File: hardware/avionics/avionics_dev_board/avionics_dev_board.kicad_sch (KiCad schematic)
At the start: 78 parts, among them IC1 ADXL375BCCZ, IC2 W25Q256JVEIQ, J1 Main battery, J10 Parachute battery, J2 LAMBDA62, J3 Conn_01x08_Socket, J4 LAMBDA80, J5 Conn_01x08_Socket, J6 SWD interface, J7 868MHz antenna, J8 2.4GHz antenna, J9 Nichrome connector, Q1 Q_NMOS, SW1 SW_Push, SW2 SW_Push, SW3 SW_Push, SW4 SW_Push, U1 TPS563200, U2 MMC5983MA, U3 LSM6DSR, U4 BMP581, U6 MAX-M10S-00B, U7 STM32G474RET6, Y1 8MHz

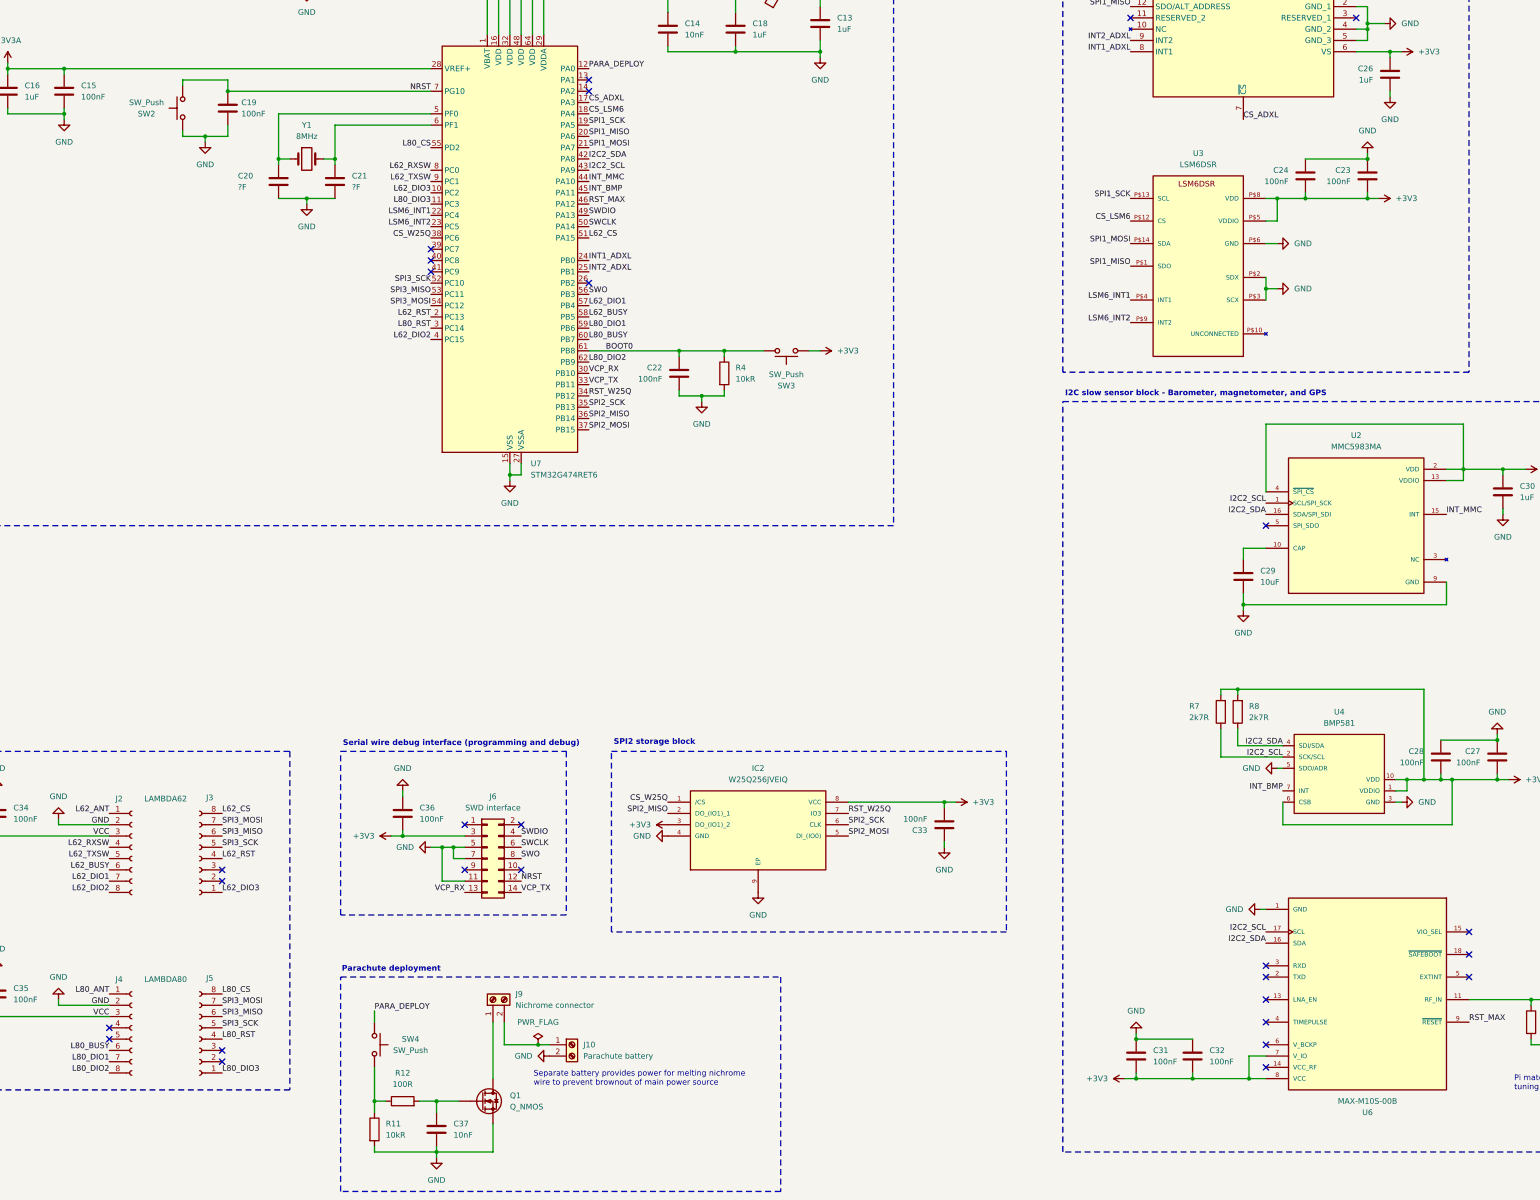
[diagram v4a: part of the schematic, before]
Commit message: Updated component selections and footprints assigned
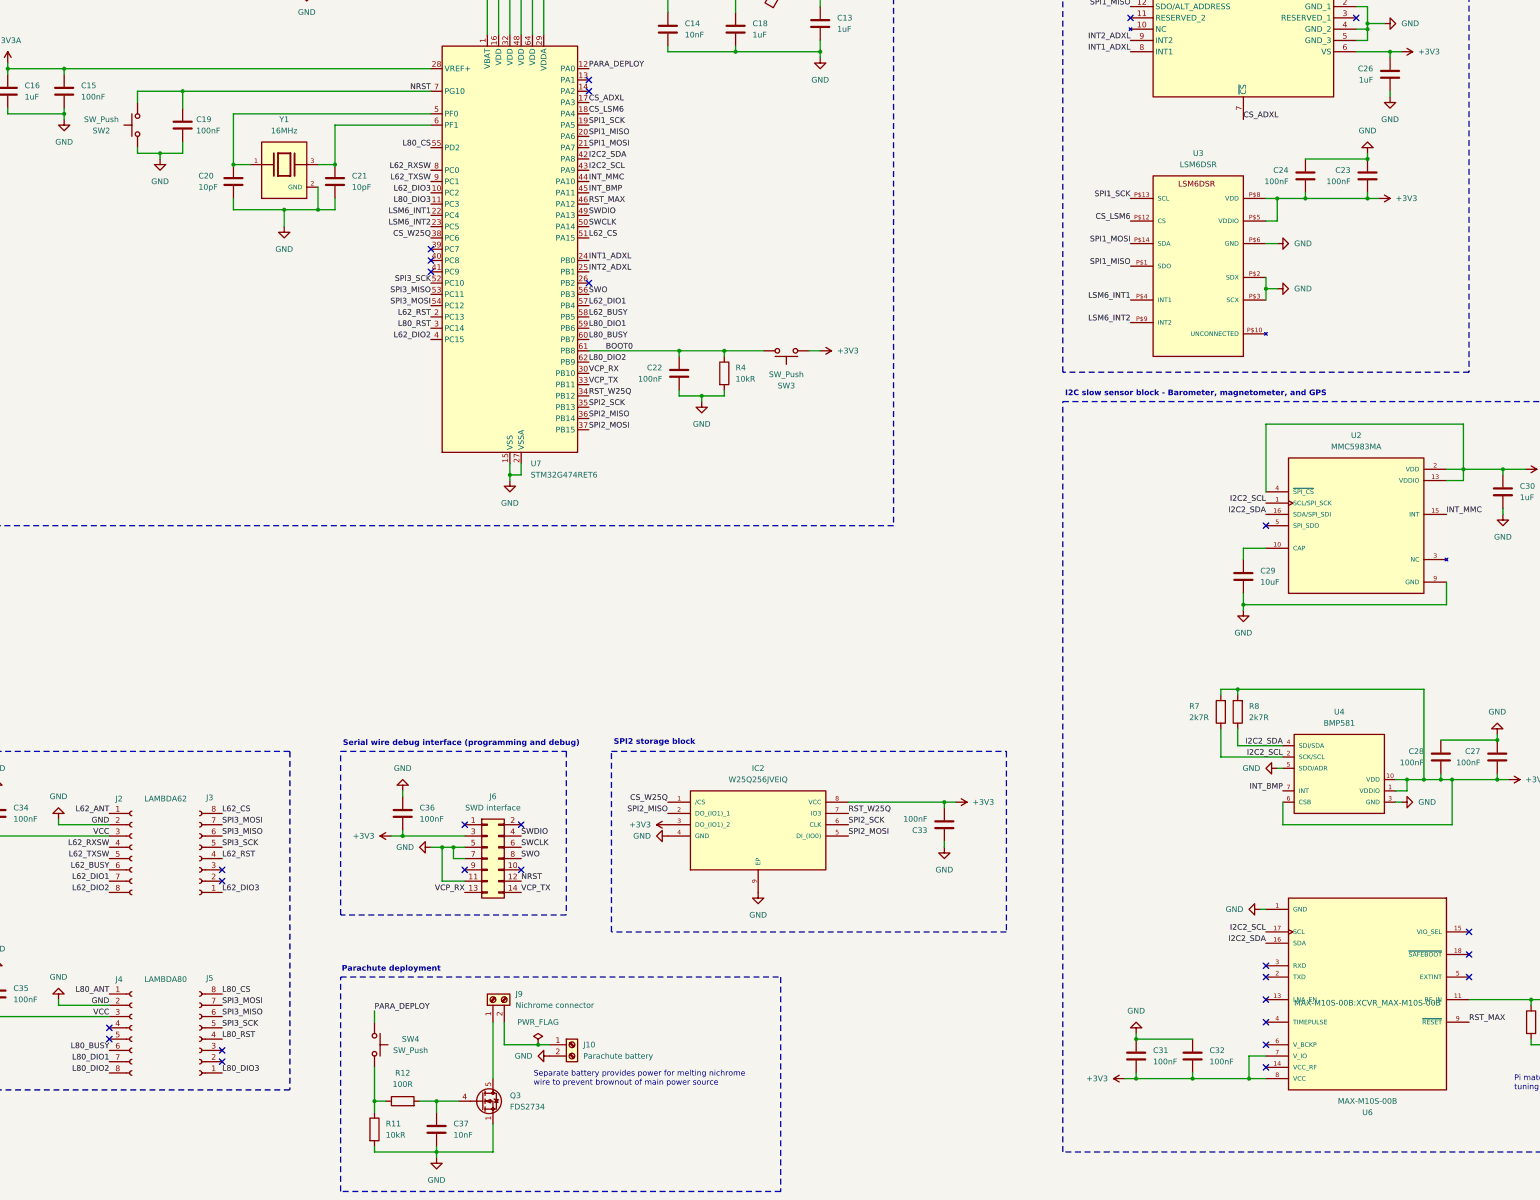
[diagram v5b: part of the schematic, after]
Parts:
- removed Q1: Q_NMOS, symbol Device:Q_NMOS
- removed Y1: 8MHz, symbol Device:Crystal
- added Q3: FDS2734, Package_SO:SOIC-8_3.9x4.9mm_P1.27mm, symbol Transistor_FET:FDS2734
- added Y1: 16MHz, ABM8G-16.000MHZ-4Y-T3:XTAL_ABM8G-16.000MHZ-4Y-T3, symbol ABM8G-16.000MHZ-4Y-T3:ABM8G-16.000MHZ-4Y-T3
- C1, C2, C8, C9: footprint Capacitor_SMD:C_0603_1608Metric -> Capacitor_SMD:C_0805_2012Metric
- C10, C11, C12, C13, C14, C15, C16, C17, C18, C19, C22, C23, C24, C25, C26, C27, C28, C29, C30, C31, C32, C33, C34, C35, C36, C37, C5: footprint (none) -> Capacitor_SMD:C_0603_1608Metric
- C20, C21: value ?F -> 10pF; footprint (none) -> Capacitor_SMD:C_0603_1608Metric
- C6: footprint (none) -> Capacitor_SMD:C_0805_2012Metric
- D1: footprint (none) -> LED_SMD:LED_0603_1608Metric
- D2: footprint (none) -> Diode_SMD:D_SOD-123F
- F1: footprint (none) -> Fuse:Fuse_0603_1608Metric
- FB1: footprint (none) -> Inductor_SMD:L_0603_1608Metric
- IC1: footprint (none) -> ADXL375:CC-14-1
- J6: footprint (none) -> Connector_PinHeader_2.54mm:PinHeader_2x07_P2.54mm_Vertical
- J7, J8: footprint (none) -> Connector_Coaxial:SMA_Amphenol_901-144_Vertical
- L1: footprint Inductor_SMD:L_Coilcraft_1515SQ-68N -> Inductor_SMD:L_0805_2012Metric
- R11, R12, R13, R14, R15, R4, R7, R8: footprint (none) -> Resistor_SMD:R_0603_1608Metric
- SW2: footprint Button_Switch_SMD:SW_DIP_SPSTx01_Slide_6.7x4.1mm_W6.73mm_P2.54mm_LowProfile_JPin -> Button_Switch_SMD:SW_SPST_B3U-1000P
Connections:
- net GND: now also Q3.1 (S), Q3.2 (S), Q3.3 (S), Y1.2 (GND), Y1.4 (GND)
- net at J9.1 (Pin_1): now also Q3.5 (D), Q3.6 (D), Q3.7 (D), Q3.8 (D)
- net at C37.1, R12.2: now also Q3.4 (G)
- net at C20.1, U7.5 (PF0): now also Y1.1
- net at C21.1, U7.6 (PF1): now also Y1.3
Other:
- moved on the sheet: C19, C20, SW2

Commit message: First revision of avionics dev board PCB - needs routing fixes
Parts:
- removed SW1, SW3: SW_Push, Button_Switch_SMD:SW_DIP_SPSTx01_Slide_6.7x4.1mm_W6.73mm_P2.54mm_LowProfile_JPin, symbol Switch:SW_Push
- removed SW2: SW_Push, Button_Switch_SMD:SW_SPST_B3U-1000P, symbol Switch:SW_Push
- added SW2, SW3, SW5: SW_SPDT, avionicsw:SHOU HAN SS12D10G5, symbol Switch:SW_SPDT
- F1: value 2A -> 1A
- SW4: footprint Button_Switch_SMD:SW_DIP_SPSTx01_Slide_6.7x4.1mm_W6.73mm_P2.54mm_LowProfile_JPin -> avionicsw:G-Switch GT-TC060A-H025-L1S
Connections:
- net +3V3: now also U7.1 (VBAT), U7.16 (VDD), U7.32 (VDD), U7.48 (VDD), U7.64 (VDD), SW2.2 (B)
- net BOOT0: now also SW2.3 (C)
- net GND: now also SW4.1; no longer U7.1 (VBAT), U7.16 (VDD), U7.32 (VDD), U7.48 (VDD), U7.64 (VDD)
- net NRST: now also SW4.2
- net PARA_DEPLOY: now also SW3.2 (B); no longer SW4.1
- net at C3.2, D2.1 (K): now also U1.3 (VIN), U1.5 (EN)
- net at C1.2, F1.1: now also SW5.1 (A); no longer J1.2 (Pin_2)
- net at R11.1, R12.1: now also SW3.3 (C); no longer SW4.2
- new net: J1.2 (Pin_2), SW5.2 (B)
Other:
- moved on the sheet: C1, C10, C11, C12, C17, C2, C3, C5, C6, D2, F1, J1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

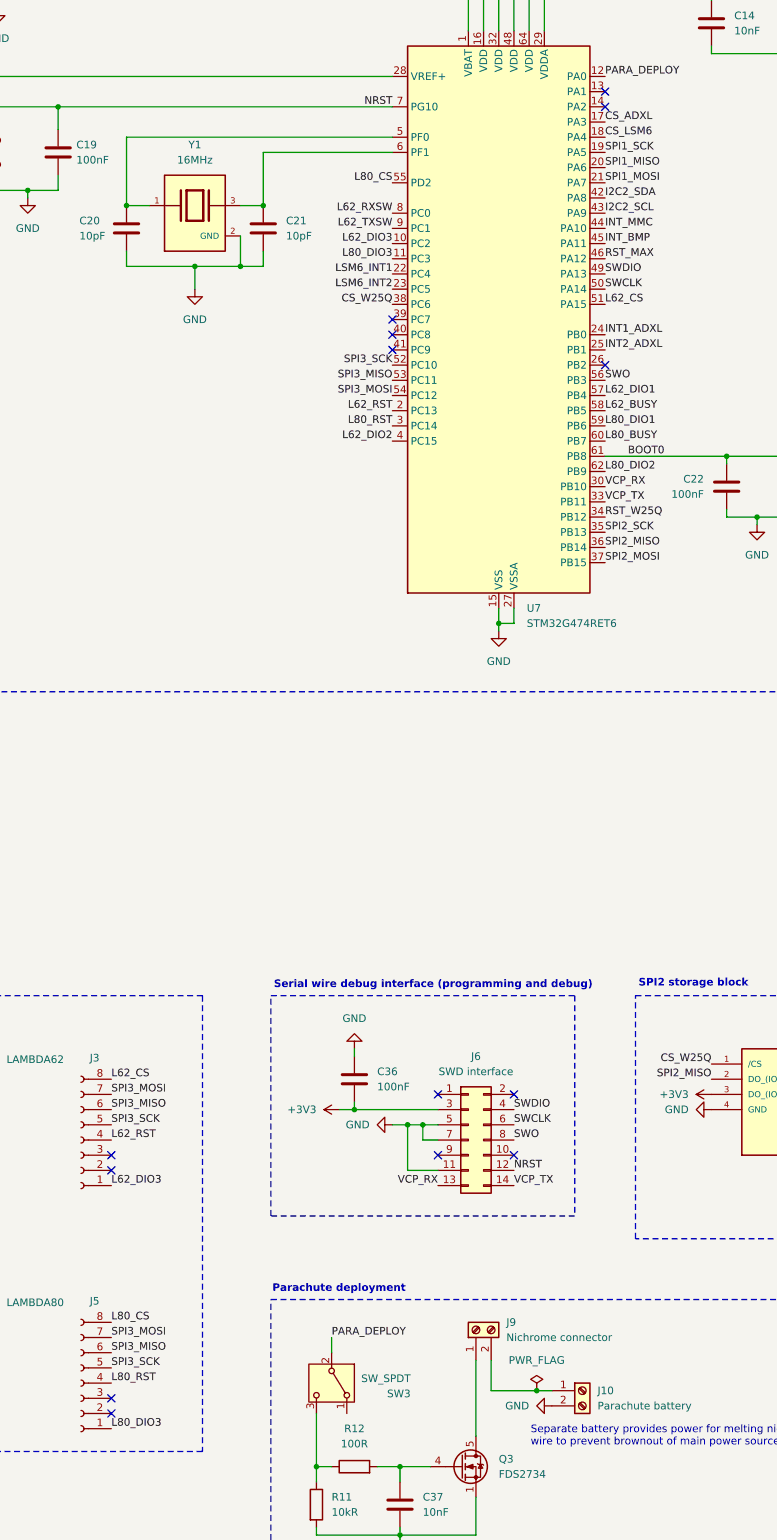
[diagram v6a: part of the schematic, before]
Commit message: Avionics dev PCB revision 2 - improved stackup and routing
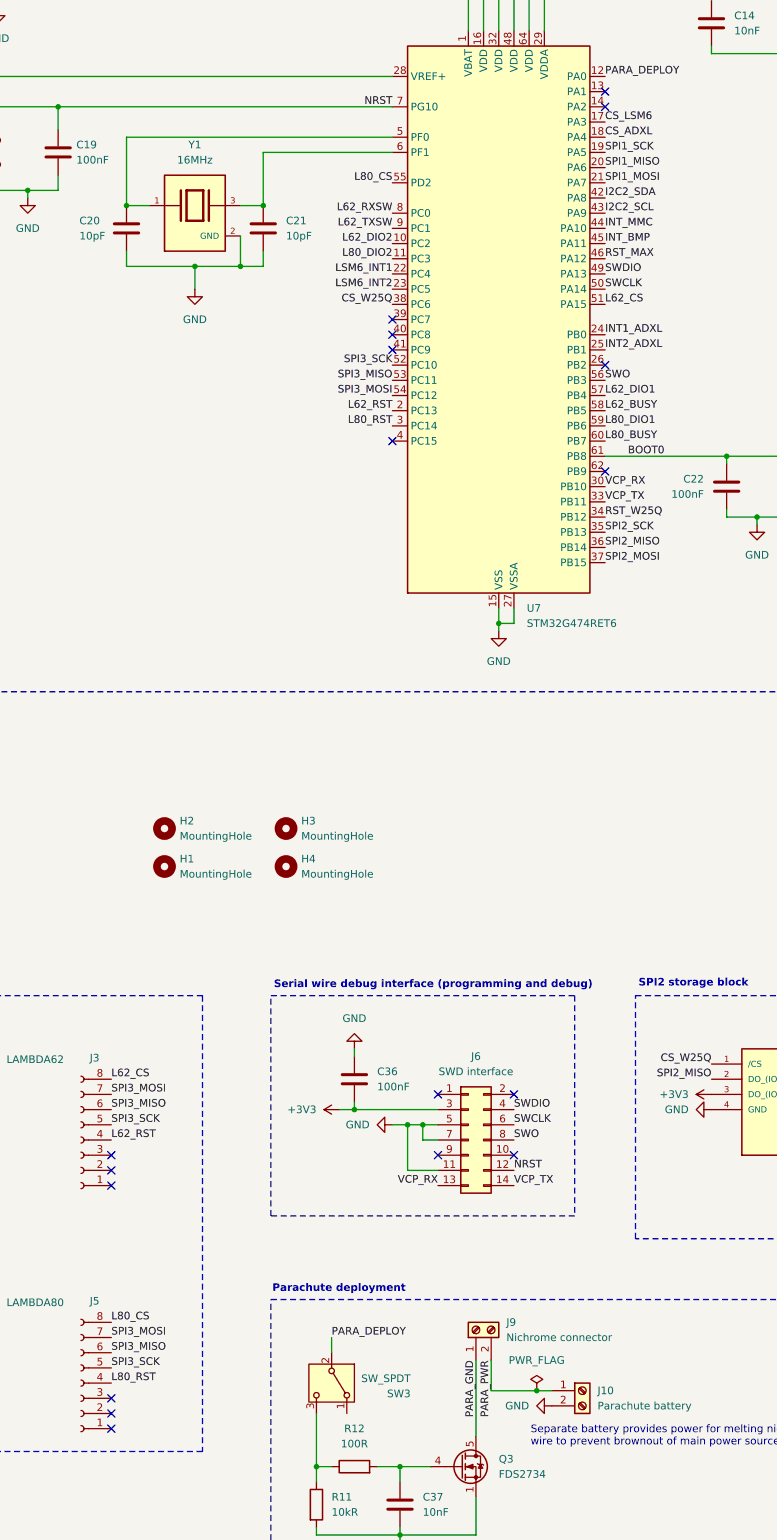
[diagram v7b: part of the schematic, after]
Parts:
- added H1, H2, H3, H4: MountingHole, MountingHole:MountingHole_2.2mm_M2, symbol Mechanical:MountingHole
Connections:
- net CS_ADXL: now also U7.18 (PA4); no longer U7.17 (PA3)
- net CS_LSM6: now also U7.17 (PA3); no longer U7.18 (PA4)
- net L62_DIO2: now also U7.10 (PC2); no longer U7.4 (PC15)
- net L80_DIO2: now also U7.11 (PC3); no longer U7.62 (PB9)
- net PARA_GND: now reaches J9.1 (Pin_1), Q3.5 (D), Q3.6 (D), Q3.7 (D), Q3.8 (D)
- net PARA_PWR: now reaches J10.1 (Pin_1), J9.2 (Pin_2)
- net L62_DIO3: no longer names the net of J3.1 (Pin_1)
- net L62_DIO3: no longer U7.10 (PC2)
- net L80_DIO3: no longer names the net of J5.1 (Pin_1)
- net L80_DIO3: no longer U7.11 (PC3)
- no-connect marks 28 -> 32

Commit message: Cleanup and refinements to avionics dev board PCB
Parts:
- added TP1, TP10, TP11, TP2, TP3, TP4, TP5, TP6, TP7, TP8, TP9: TestPoint, TestPoint:TestPoint_Pad_D1.0mm, symbol Connector:TestPoint
- renumbered IC1 to ADXL1, J8 to ANT_24, J7 to ANT_868, U4 to BMP1, SW2 to BOOT_SW1, U1 to BUCK1, J1 to J1-MBAT1, J10 to J10-PBAT1, J9 to J9-NICH1, J2 to L62-1, J3 to L62-2, J4 to L80-1, J5 to L80-2, U3 to LSM6, U6 to M10S1, U7 to MCU1, U2 to MMC1, SW3 to PARA_ARM1, D1 to PWR_LED1, SW5 to PWR_SW1, SW4 to RST1, J6 to SWD_INT1, IC2 to W25Q1
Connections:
- no-connect marks 32 -> 35
